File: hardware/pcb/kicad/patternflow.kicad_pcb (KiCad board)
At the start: 2 copper layers, 74 x 132.5 mm, 11 parts, among them J1 Conn_02x08_Odd_Even, J3 Screw_Terminal_01x02, SW1 RotaryEncoder_Switch, SW2 RotaryEncoder_Switch, SW3 RotaryEncoder_Switch, SW4 RotaryEncoder_Switch, U1 ESP32-S3-DevKit-44pin

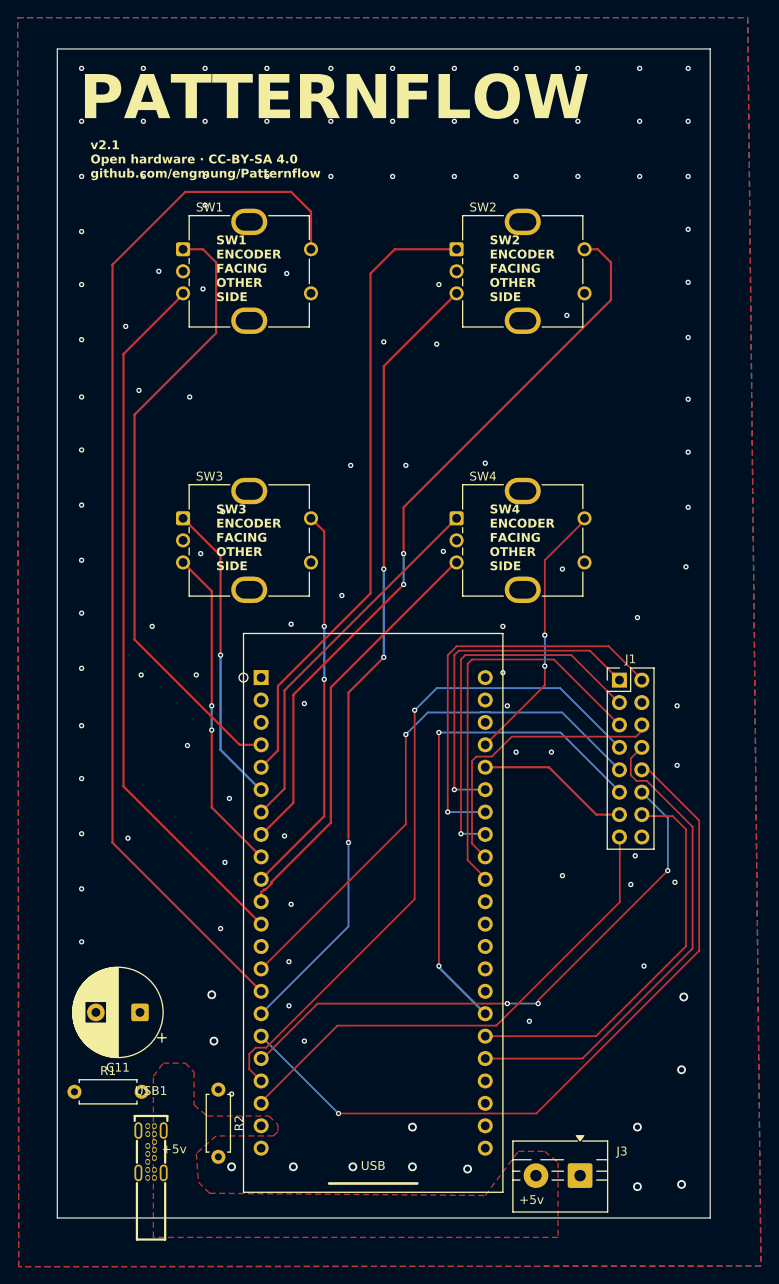
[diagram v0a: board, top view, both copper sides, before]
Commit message: feat(pcb): v2.2 USB Type-C power input, SMD-free board
Rework the board per the power-supply change in #114:
- Switch power input to USB Type-C (SHOU HAN TYPE-C 14P CC-2.6,
  LCSC C5187475); add its footprint and 3D models.
- Remove all SMD passives; the two 5.1k USB-C CC pull-downs are
  hand-soldered, so the whole board is hand-solderable.
- Move the Type-C connector toward center for easier cable insertion.
- Reduce overall board size; bump silkscreen to v2.2.

Generate fab output patternflow_v2.2_test_gerber.zip (DRC clean: 0
violations / 0 unconnected). The _test suffix stays until a fabricated
board is verified.

Refs #114

Co-Authored-By: Claude Opus 4.8 <noreply@anthropic.com>
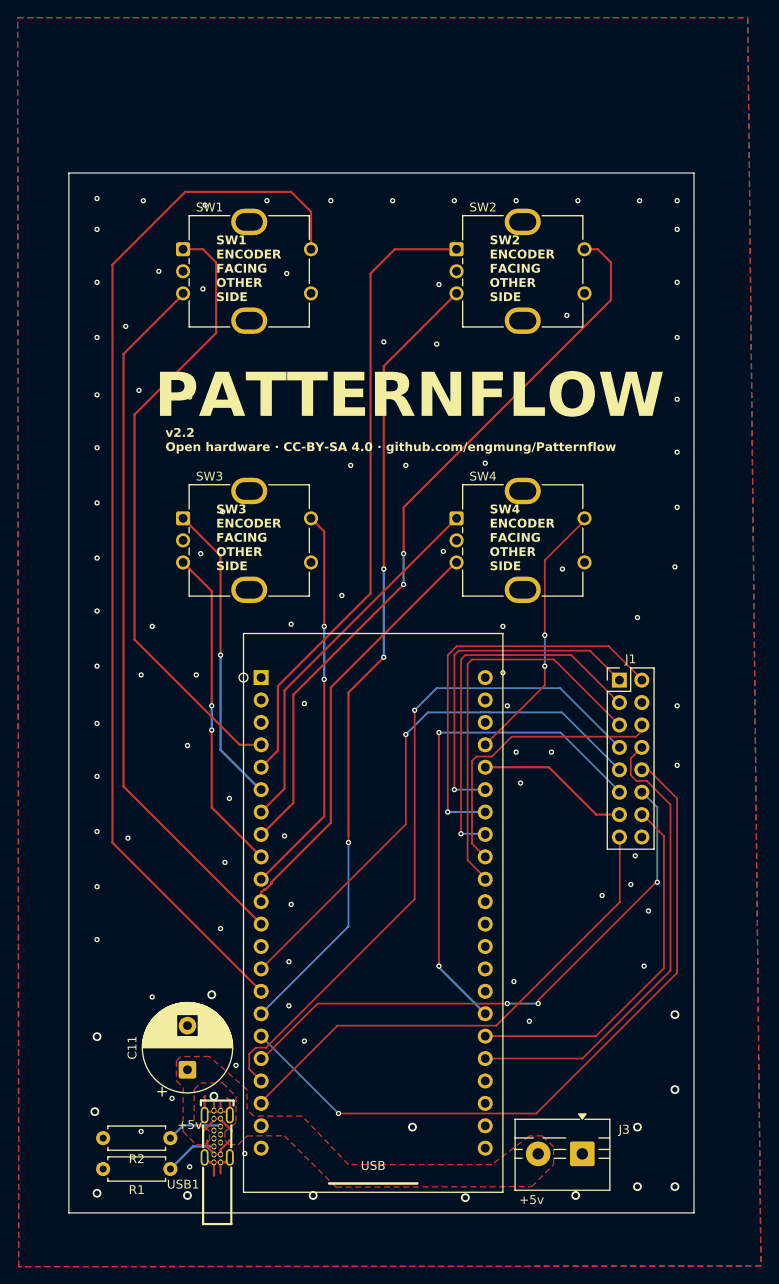
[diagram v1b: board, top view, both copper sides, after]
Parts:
- moved R1 14.0 mm to (66.8, 155.8), turned to 180 degrees
- moved C11 8.44 mm to (68.8, 144.5), turned to 90 degrees
- moved R2 7.74 mm to (66.8, 152.2), turned to 180 degrees
- moved USB1 7.70 mm to (72.1, 152.1)
- moved J3 2.48 mm to (113.5, 154.0)
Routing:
- net GND: track 0.00 -> 15.5 mm, vias 116 -> 102
- net +5V: track 0.00 -> 9.38 mm
- net Net-(USB1-CC2): track 0.00 -> 6.34 mm
- net Net-(USB1-CC1): track 0.00 -> 6.00 mm
- net /HUB_LAT: track 45.9 -> 41.9 mm
- net /HUB_E: track 55.6 -> 53.5 mm
- net /HUB_B: track 84.6 -> 82.5 mm
- net /HUB_D: track 65.3 -> 64.4 mm
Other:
- board size 74 x 132.5 mm -> 70.9 x 117.9 mm
- board text added: "v2.2 Open hardware · CC-BY-SA 4.0 · github.com/engmung/Patternflow"
- board text removed: "v2.1 Open hardware · CC-BY-SA 4.0 github.com/engmung/Patternflow"

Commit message: hardware(pcb): v3.0 test board — hybrid power input (USB-C + 2-pin screw terminal)
Per the plan in issue #114: instead of splitting into two PCBs, one board now
carries both power-input options.

- Add a 2-pin screw terminal footprint on the back as a beginner-friendly
  bypass for the difficult USB-C THT soldering (strip a USB cable, screw it in)
- Clean up routing
- Bump silkscreen version text to v3.0
- Bake v3.0 test Gerbers (DRC clean: 0 violations, 0 unconnected) into
  hardware/pcb/gerber/experiment/ with a do-not-order README
- Delete patternflow_v2.2_test_gerber.zip so nobody orders the superseded
  test revision by mistake; BUILD_GUIDE warning updated to match

Co-Authored-By: Claude Opus 4.8 <noreply@anthropic.com>
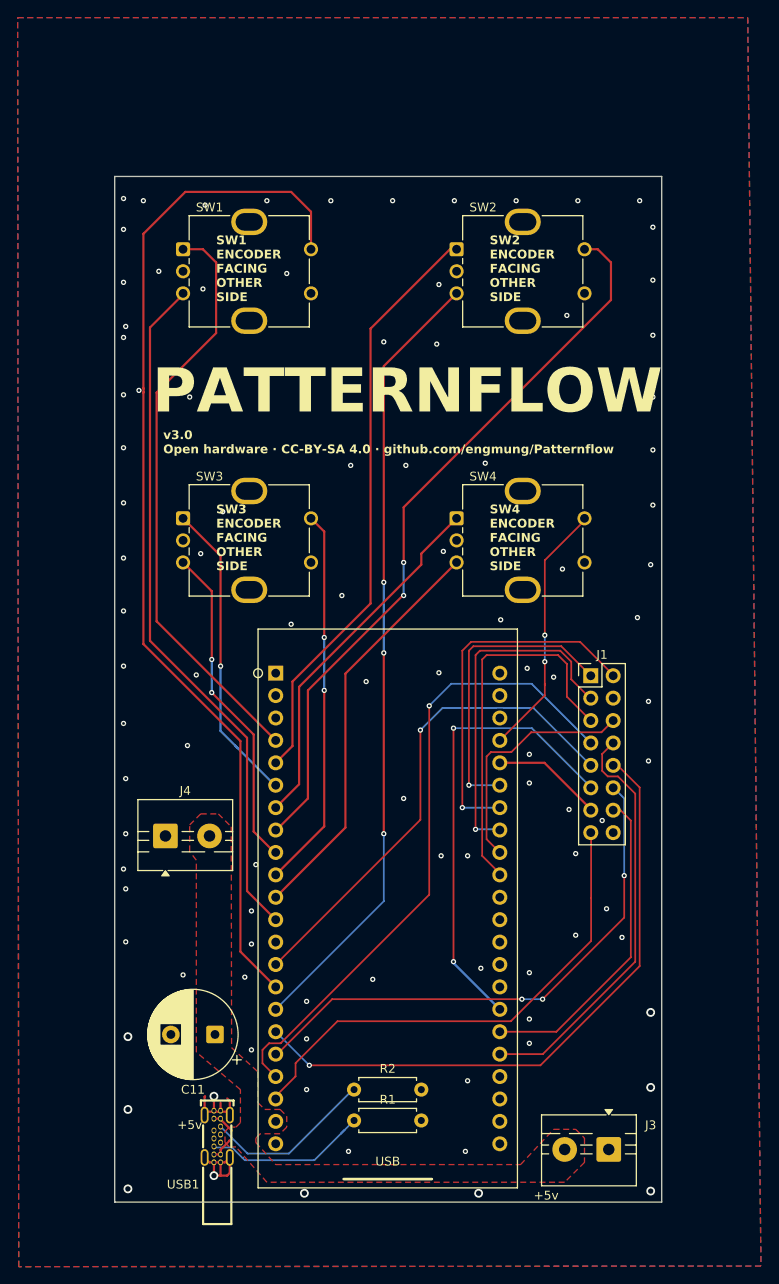
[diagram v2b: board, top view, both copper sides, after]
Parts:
- added J4: Screw_Terminal_01x02, TerminalBlock:TerminalBlock_MaiXu_MX126-5.0-02P_1x02_P5.00mm, F.Cu at (66.2, 118.0)
- moved R1 21.5 mm to (87.6, 150.2), turned to 0 degrees
- moved R2 21.5 mm to (87.6, 146.8), turned to 0 degrees
- moved C11 5.07 mm to (71.9, 140.5), turned to 180 degrees
- moved J1 3.29 mm to (114.5, 99.8)
- moved J3 3.04 mm to (116.5, 153.5)
- moved U1 1.72 mm to (91.5, 126.2)
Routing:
- net Net-(USB1-CC2): track 6.34 -> 20.3 mm
- net Net-(USB1-CC1): track 6.00 -> 19.0 mm
- net /HUB_B: track 82.5 -> 71.8 mm
- net /HUB_E: track 53.5 -> 47.2 mm
- net /HUB_LAT: track 41.9 -> 36.3 mm
- net /HUB_G2: track 32.8 -> 27.5 mm
- net /HUB_R1: track 39.1 -> 34.2 mm
- net /HUB_G1: track 46.1 -> 41.2 mm
- net /HUB_C: track 57.8 -> 52.9 mm
- net /HUB_A: track 61.3 -> 56.5 mm
- net /ENC2_A: track 72.0 -> 67.1 mm
- net /HUB_CLK: track 17.4 -> 12.6 mm
- net /HUB_B2: track 78.1 -> 73.4 mm
- net GND: track 15.5 -> 19.4 mm, vias 102 -> 99
- net /HUB_B1: track 42.9 -> 39.2 mm
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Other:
- board size 70.9 x 117.9 mm -> 62 x 116.2 mm
- board text added: "v3.0 Open hardware · CC-BY-SA 4.0 · github.com/engmung/Patternflow"
- board text removed: "v2.2 Open hardware · CC-BY-SA 4.0 · github.com/engmung/Patternflow"

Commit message: fix(pcb): correct C11 value typo 1000uF/1.6V -> 1000uF/16V
The part is a 16V Rubycon PX (16PX1000MEFC10X12.5); the schematic
value read 1.6V, which would be under-spec on the 5V rail.

Co-Authored-By: Claude Fable 5 <noreply@anthropic.com>
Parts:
- C11: value 1000uF/1.6V -> 1000uF/16V
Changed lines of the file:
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@@
 			)
 		)
-		(property "Value" "1000uF/1.6V"
+		(property "Value" "1000uF/16V"
 			(at 2.5 6.25 0)
 			(layer "F.Fab")
